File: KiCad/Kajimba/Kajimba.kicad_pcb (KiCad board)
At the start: 2 copper layers, 66.5 x 43.7 mm, 19 parts, among them J1 Barrel Jack, J2 Pump, J3 Sensor, J4 Screen, J5 Button, Q1 QM6006D, SW1 Button, U1 Pico, U2 LM78M05

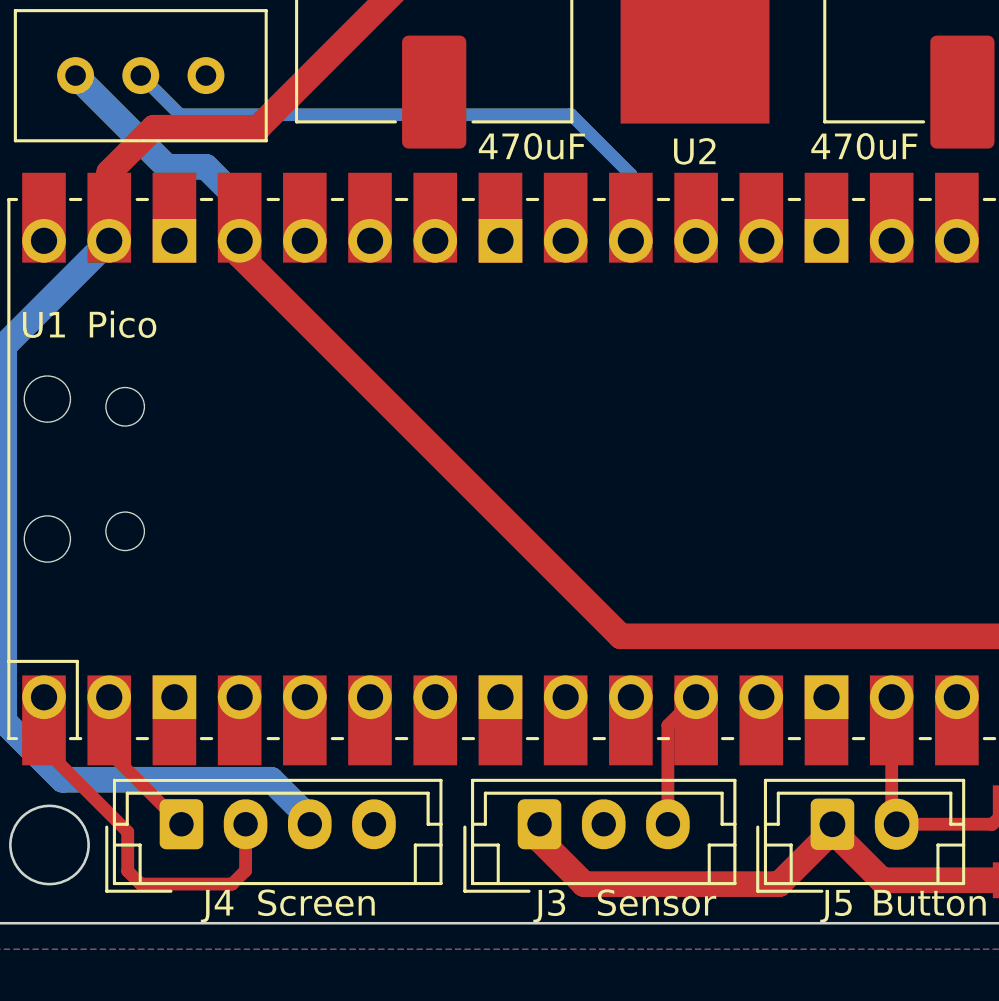
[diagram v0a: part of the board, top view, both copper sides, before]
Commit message: v05
moved pin 3.3v_en to 3.3v
switched pins on 3 pin jst connector
cleaned up circuit diagram sheet
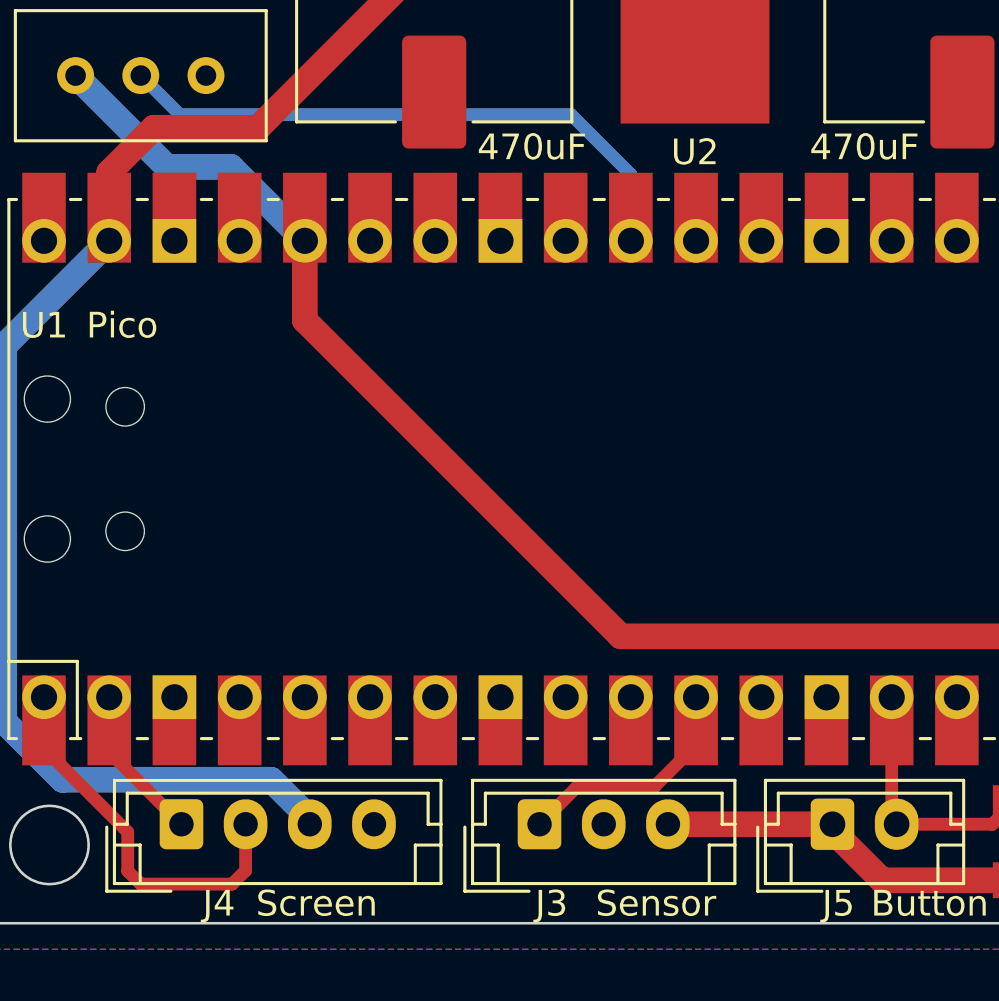
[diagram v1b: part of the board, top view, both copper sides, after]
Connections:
- J3 pad 1: +3.3V -> Sensor
- J3 pad 3: Sensor -> +3.3V
- U1 pad 26: Relay -> unconnected-(U1-Pad26)
- U1 pad 36: unconnected-(U1-Pad36) -> +3.3V
- U1 pad 37: +3.3V -> unconnected-(U1-Pad37)
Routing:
- net +3.3V: track 103.7 -> 97.1 mm
- net Sensor: track 5.40 -> 9.24 mm
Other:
- board text added: "v05 Kajimba Pump"
- board text removed: "v04 Kajimba Pump"
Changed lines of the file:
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@@
   )
   (paper "A4")
+  (title_block
+    (title "Pump")
+    (date "2022-12-22")
+    (rev "v05")
+    (company "Kajimba")
+    (comment 1 "Author: Yael")
+  )
   (layers
     (0 "F.Cu" signal)
@@
   (net 3 "+5V")
   (net 4 "Net-(D2-Pad2)")
-  (net 5 "Relay")
+  (net 5 "unconnected-(U1-Pad26)")
   (net 6 "+12V")
   (net 7 "unconnected-(J1-Pad3)")
@@
   (net 35 "unconnected-(U1-Pad34)")
   (net 36 "unconnected-(U1-Pad35)")
-  (net 37 "unconnected-(U1-Pad36)")
+  (net 37 "unconnected-(U1-Pad37)")
   (net 38 "unconnected-(U1-Pad40)")
   (net 39 "unconnected-(U1-Pad41)")
@@
       (net 8 "PWM") (pinfunction "GPIO19") (pintype "bidirectional"))
     (pad "26" smd rect (at 8.89 11.43 90) (size 3.5 1.7) (drill (offset 0.9 0)) (layers "F.Cu" "F.Mask")
-      (net 5 "Relay") (pinfunction "GPIO20") (pintype "bidirectional"))
+      (net 5 "unconnected-(U1-Pad26)") (pinfunction "GPIO20") (pintype "bidirectional"))
     (pad "26" thru_hole oval (at 8.89 11.43 90) (size 1.7 1.7) (drill 1.02) (layers *.Cu *.Mask)
-      (net 5 "Relay") (pinfunction "GPIO20") (pintype "bidirectional"))
+      (net 5 "unconnected-(U1-Pad26)") (pinfunction "GPIO20") (pintype "bidirectional"))
     (pad "27" smd rect (at 8.89 8.89 90) (size 3.5 1.7) (drill (offset 0.9 0)) (layers "F.Cu" "F.Mask")
       (net 29 "unconnected-(U1-Pad27)") (pinfunction "GPIO21") (pintype "bidirectional"))
@@
       (net 36 "unconnected-(U1-Pad35)") (pinfunction "ADC_VREF") (pintype "power_in"))
     (pad "36" smd rect (at 8.89 -13.97 90) (size 3.5 1.7) (drill (offset 0.9 0)) (layers "F.Cu" "F.Mask")
-      (net 37 "unconnected-(U1-Pad36)") (pinfunction "3V3") (pintype "power_in"))
+      (net 9 "+3.3V") (pinfunction "3V3") (pintype "power_in"))
     (pad "36" thru_hole oval (at 8.89 -13.97 90) (size 1.7 1.7) (drill 1.02) (layers *.Cu *.Mask)
-      (net 37 "unconnected-(U1-Pad36)") (pinfunction "3V3") (pintype "power_in"))
+      (net 9 "+3.3V") (pinfunction "3V3") (pintype "power_in"))
     (pad "37" smd rect (at 8.89 -16.51 90) (size 3.5 1.7) (drill (offset 0.9 0)) (layers "F.Cu" "F.Mask")
-      (net 9 "+3.3V") (pinfunction "3V3_EN") (pintype "input"))
+      (net 37 "unconnected-(U1-Pad37)") (pinfunction "3V3_EN") (pintype "input"))
     (pad "37" thru_hole oval (at 8.89 -16.51 90) (size 1.7 1.7) (drill 1.02) (layers *.Cu *.Mask)
-      (net 9 "+3.3V") (pinfunction "3V3_EN") (pintype "input"))
+      (net 37 "unconnected-(U1-Pad37)") (pinfunction "3V3_EN") (pintype "input"))
     (pad "38" smd rect (at 8.89 -19.05 90) (size 3.5 1.7) (drill (offset 0.9 0)) (layers "F.Cu" "F.Mask")
       (net 2 "GND") (pinfunction "GND") (pintype "bidirectional"))
@@
     (fp_line (start -2.5 2.2) (end 7.5 2.2) (layer "F.Fab") (width 0.1))
     (pad "1" thru_hole roundrect (at 0 0) (size 1.7 1.95) (drill 0.95) (layers *.Cu *.Mask) (roundrect_rratio 0.1470588235)
-      (net 9 "+3.3V") (pinfunction "Pin_1") (pintype "passive"))
+      (net 10 "Sensor") (pinfunction "Pin_1") (pintype "passive"))
     (pad "2" thru_hole oval (at 2.5 0) (size 1.7 1.95) (drill 0.95) (layers *.Cu *.Mask)
       (net 2 "GND") (pinfunction "Pin_2") (pintype "passive"))
     (pad "3" thru_hole oval (at 5 0) (size 1.7 1.95) (drill 0.95) (layers *.Cu *.Mask)
-      (net 10 "Sensor") (pinfunction "Pin_3") (pintype "passive"))
+      (net 9 "+3.3V") (pinfunction "Pin_3") (pintype "passive"))
     (model "${KICAD6_3DMODEL_DIR}/Connector_JST.3dshapes/JST_EH_B3B-EH-A_1x03_P2.50mm_Vertical.wrl"
       (offset (xyz 0 0 0))
@@
   (gr_circle (center 160.528 82.55) (end 162.052 82.55) (layer "Edge.Cuts") (width 0.1) (fill none))
   (gr_circle (center 115.824 120.396) (end 117.348 120.396) (layer "Edge.Cuts") (width 0.1) (fill none))
-  (gr_text "v04 Kajimba Pump" (at 143.764 105.664 180) (layer "B.SilkS")
+  (gr_text "v05 Kajimba Pump" (at 143.764 105.664 180) (layer "B.SilkS")
     (effects (font (size 1.5 1.5) (thickness 0.3)) (justify mirror))
   )
@@
   (segment (start 178.308 109.728) (end 174.244 109.728) (width 0.5) (layer "F.Cu") (net 8))
   (segment (start 138.078 112.268) (end 164.592 112.268) (width 1) (layer "F.Cu") (net 9))
+  (segment (start 146.324 119.588) (end 139.914 119.588) (width 1) (layer "F.Cu") (net 9))
   (segment (start 166.624 121.412) (end 165.608 122.428) (width 1) (layer "F.Cu") (net 9))
+  (segment (start 125.771 99.961) (end 125.771 96.861) (width 1) (layer "F.Cu") (net 9))
   (segment (start 146.324 119.588) (end 146.324 119.842) (width 1) (layer "F.Cu") (net 9))
-  (segment (start 134.914 120.182) (end 136.652 121.92) (width 1) (layer "F.Cu") (net 9))
-  (segment (start 123.231 97.421) (end 138.078 112.268) (width 1) (layer "F.Cu") (net 9))
   (segment (start 146.324 119.842) (end 148.251 121.769) (width 1) (layer "F.Cu") (net 9))
   (segment (start 165.608 122.428) (end 161.231 122.428) (width 1) (layer "F.Cu") (net 9))
-  (segment (start 136.652 121.92) (end 144.246 121.92) (width 1) (layer "F.Cu") (net 9))
-  (segment (start 134.914 119.588) (end 134.914 120.182) (width 1) (layer "F.Cu") (net 9))
   (segment (start 161.231 122.428) (end 160.572 121.769) (width 1) (layer "F.Cu") (net 9))
   (segment (start 166.624 114.3) (end 166.624 121.412) (width 1) (layer "F.Cu") (net 9))
-  (segment (start 123.231 96.861) (end 123.231 97.421) (width 1) (layer "F.Cu") (net 9))
   (segment (start 148.251 121.769) (end 153.372 121.769) (width 1) (layer "F.Cu") (net 9))
-  (segment (start 146.324 119.842) (end 144.246 121.92) (width 1) (layer "F.Cu") (net 9))
+  (segment (start 138.078 112.268) (end 125.771 99.961) (width 1) (layer "F.Cu") (net 9))
   (segment (start 164.592 112.268) (end 166.624 114.3) (width 1) (layer "F.Cu") (net 9))
   (segment (start 160.572 121.769) (end 153.372 121.769) (width 1) (layer "F.Cu") (net 9))
-  (segment (start 123.231 95.291) (end 123.231 96.861) (width 1) (layer "B.Cu") (net 9))
-  (segment (start 121.92 93.98) (end 123.231 95.291) (width 1) (layer "B.Cu") (net 9))
-  (segment (start 120.396 93.98) (end 121.92 93.98) (width 1) (layer "B.Cu") (net 9))
+  (segment (start 122.89 93.98) (end 125.771 96.861) (width 1) (layer "B.Cu") (net 9))
   (segment (start 116.84 90.424) (end 120.396 93.98) (width 1) (layer "B.Cu") (net 9))
-  (segment (start 139.914 115.738) (end 141.011 114.641) (width 0.5) (layer "F.Cu") (net 10))
-  (segment (start 139.914 119.588) (end 139.914 115.738) (width 0.5) (layer "F.Cu") (net 10))
+  (segment (start 120.396 93.98) (end 122.89 93.98) (width 1) (layer "B.Cu") (net 9))
+  (segment (start 141.011 116.500022) (end 141.011 114.641) (width 0.5) (layer "F.Cu") (net 10))
+  (segment (start 134.914 119.588) (end 136.392 118.11) (width 0.5) (layer "F.Cu") (net 10))
+  (segment (start 139.401022 118.11) (end 141.011 116.500022) (width 0.5) (layer "F.Cu") (net 10))
+  (segment (start 136.392 118.11) (end 139.401022 118.11) (width 0.5) (layer "F.Cu") (net 10))
   (segment (start 118.151 116.775) (end 118.151 114.641) (width 0.5) (layer "F.Cu") (net 11))
   (segment (start 118.151 117.029) (end 118.151 114.641) (width 0.5) (layer "F.Cu") (net 11))
@@
     (connect_pads (clearance 0))
     (min_thickness 0.254)
-    (keepout (tracks not_allowed) (vias allowed) (pads allowed) (copperpour not_allowed) (footprints allowed))
+    (keepout (tracks not_allowed) (vias allowed) (pads allowed ) (copperpour not_allowed) (footprints allowed))
     (fill (thermal_gap 0.508) (thermal_bridge_width 0.508))
     (polygon
@@
     (connect_pads (clearance 0))
     (min_thickness 0.254)
-    (keepout (tracks not_allowed) (vias not_allowed) (pads not_allowed) (copperpour not_allowed) (footprints allowed))
+    (keepout (tracks not_allowed) (vias not_allowed) (pads not_allowed ) (copperpour not_allowed) (footprints allowed))
     (fill (thermal_gap 0.508) (thermal_bridge_width 0.508))
     (polygon

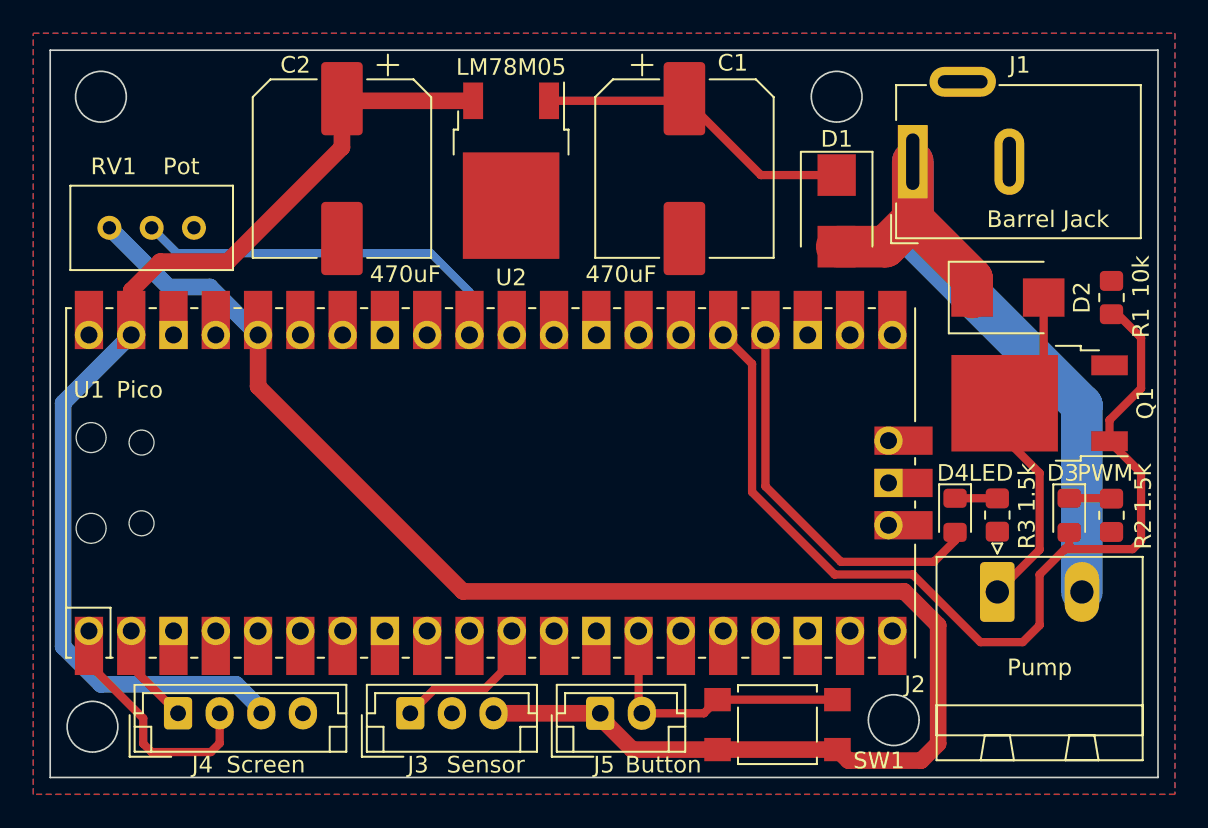
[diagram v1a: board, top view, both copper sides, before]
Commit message: v06 KiCad
removed pot
moved button / IO around
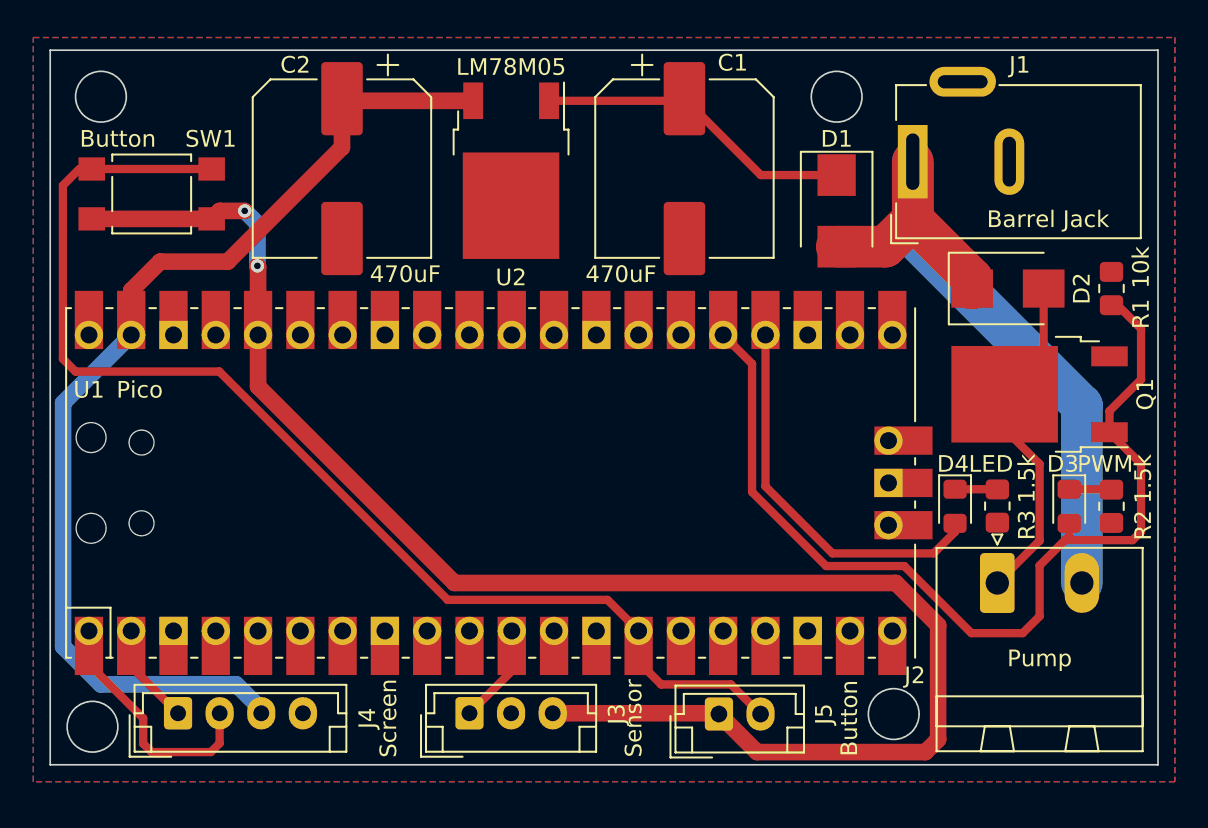
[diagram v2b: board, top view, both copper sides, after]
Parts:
- removed RV1: Pot, Potentiometer_THT:Potentiometer_Bourns_3296W_Vertical
- moved SW1 49.3 mm to (119.4, 88.4)
- moved J5 7.13 mm to (153.5, 119.6)
- moved J3 3.56 mm to (138.5, 119.6)
- moved Q1 0.54 mm to (172.7, 100.4)
- moved R3 0.54 mm to (170.2, 107.1)
- moved D2 0.54 mm to (170.8, 94.1)
- moved D3 0.54 mm to (174.5, 107.2)
- moved D4 0.54 mm to (167.6, 107.2)
- moved J2 0.54 mm to (170.2, 111.8)
- moved R1 0.54 mm to (177.0, 94.1)
- moved R2 0.54 mm to (177.0, 107.2)
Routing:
- net Button: track 17.1 -> 71.6 mm
- net Analog: track 23.3 -> 0.00 mm
- net Sensor: track 9.24 -> 6.00 mm
- net +3.3V: track 97.1 -> 98.4 mm, vias 0 -> 2
- net +12V: track 44.9 -> 43.9 mm
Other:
- board size 66.5 x 43.7 mm -> 66.5 x 42.9 mm
- board text added: "v06 Kajimba Pump"
- board text removed: "v05 Kajimba Pump"
